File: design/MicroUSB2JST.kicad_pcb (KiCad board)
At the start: 2 copper layers, 25.4 x 17.8 mm, 3 parts, among them J1 UJ2-MIBH-G-SMT-TR, J2 S2B-PH-SM4-TB_LF__SN_, J3 SM04B-SRSS-TB_LF__SN_

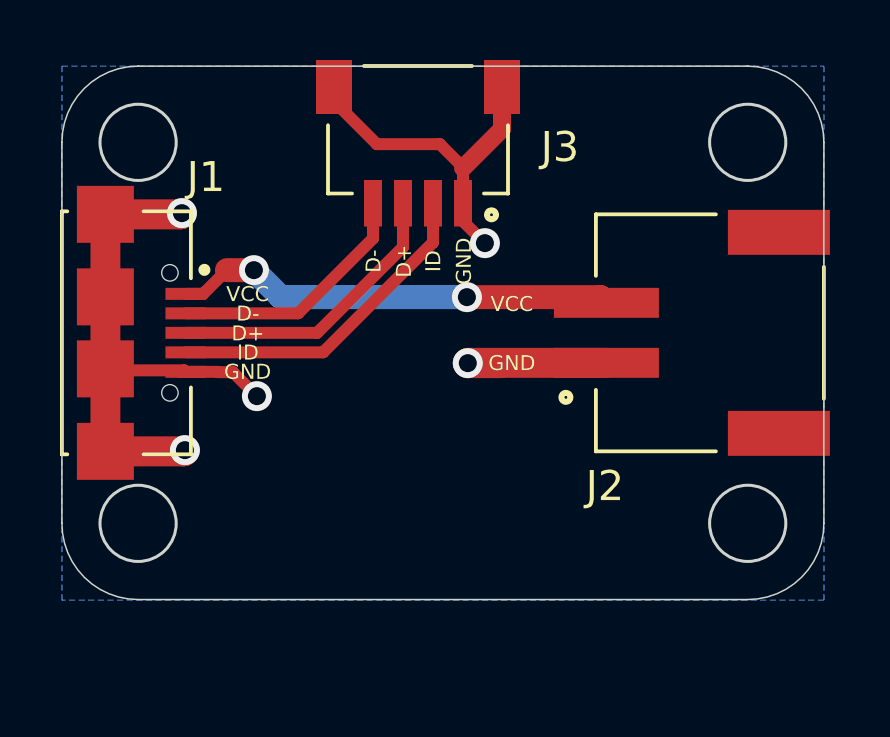
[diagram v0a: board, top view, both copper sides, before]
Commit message: best adaptation to adafruit swirly grill
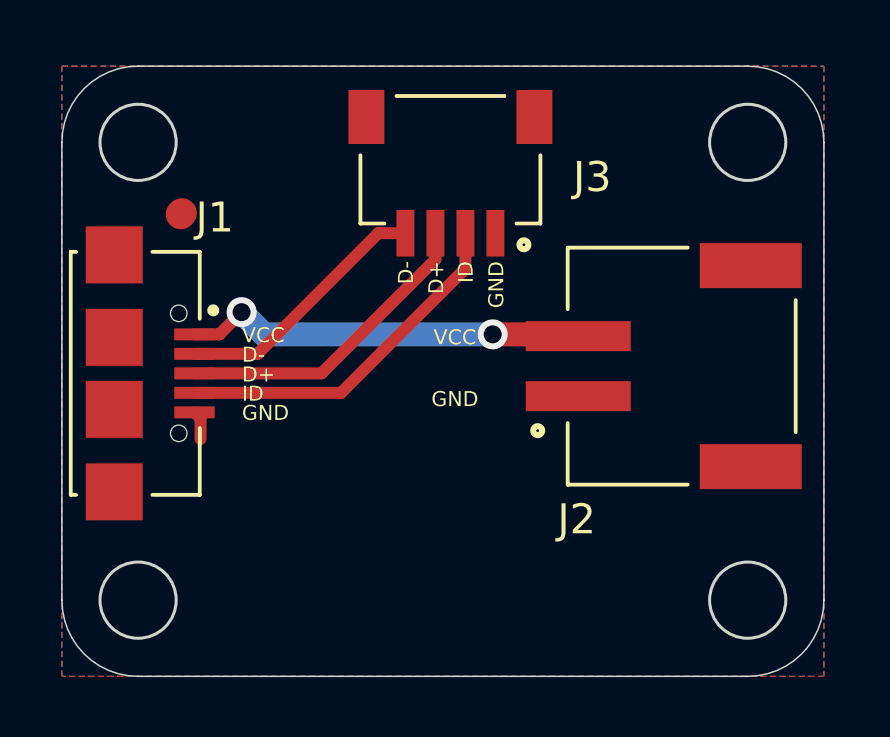
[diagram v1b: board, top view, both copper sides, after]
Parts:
- moved J3 1.47 mm to (63.0, 55.6)
- moved J2 1.45 mm to (67.2, 60.0)
- moved J1 1.38 mm to (51.7, 60.2)
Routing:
- net GND: track 36.2 -> 1.03 mm, vias 5 -> 0
- net VCC: track 14.8 -> 13.4 mm
- net ID: track 11.1 -> 11.9 mm
- net D+: track 9.89 -> 10.5 mm
- added copper zone on F.Cu, net GND
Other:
- board size 25.4 x 17.8 mm -> 25.4 x 20.3 mm
